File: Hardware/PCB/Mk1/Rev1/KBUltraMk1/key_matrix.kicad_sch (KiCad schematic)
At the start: 163 parts, among them SW1 SW_SPST, SW10 SW_SPST, SW11 SW_SPST, SW12 SW_SPST, SW13 SW_SPST, SW14 SW_SPST, SW15 SW_SPST, SW16 SW_SPST, SW17 SW_SPST, SW18 SW_SPST, SW19 SW_SPST, SW2 SW_SPST, SW20 SW_SPST, SW21 SW_SPST, SW22 SW_SPST, SW23 SW_SPST, SW24 SW_SPST, SW25 SW_SPST, SW26 SW_SPST, SW27 SW_SPST, SW28 SW_SPST, SW29 SW_SPST, SW3 SW_SPST, SW30 SW_SPST, SW31 SW_SPST, SW32 SW_SPST, SW33 SW_SPST, SW34 SW_SPST, SW35 SW_SPST, SW36 SW_SPST, SW37 SW_SPST, SW38 SW_SPST, SW39 SW_SPST, SW4 SW_SPST, SW40 SW_SPST, SW41 SW_SPST, SW42 SW_SPST, SW43 SW_SPST, SW44 SW_SPST, SW45 SW_SPST, SW46 SW_SPST, SW47 SW_SPST, SW48 SW_SPST, SW49 SW_SPST, SW5 SW_SPST, SW50 SW_SPST, SW51 SW_SPST, SW52 SW_SPST, SW53 SW_SPST, SW54 SW_SPST, SW55 SW_SPST, SW56 SW_SPST, SW57 SW_SPST, SW58 SW_SPST, SW59 SW_SPST, SW6 SW_SPST, SW60 SW_SPST, SW61 SW_SPST, SW62 SW_SPST, SW63 SW_SPST, SW64 SW_SPST, SW65 SW_SPST, SW66 SW_SPST, SW67 SW_SPST, SW68 SW_SPST, SW69 SW_SPST, SW7 SW_SPST, SW70 SW_SPST, SW71 SW_SPST, SW72 SW_SPST, SW73 SW_SPST, SW74 SW_SPST, SW75 SW_SPST, SW8 SW_SPST, SW9 SW_SPST

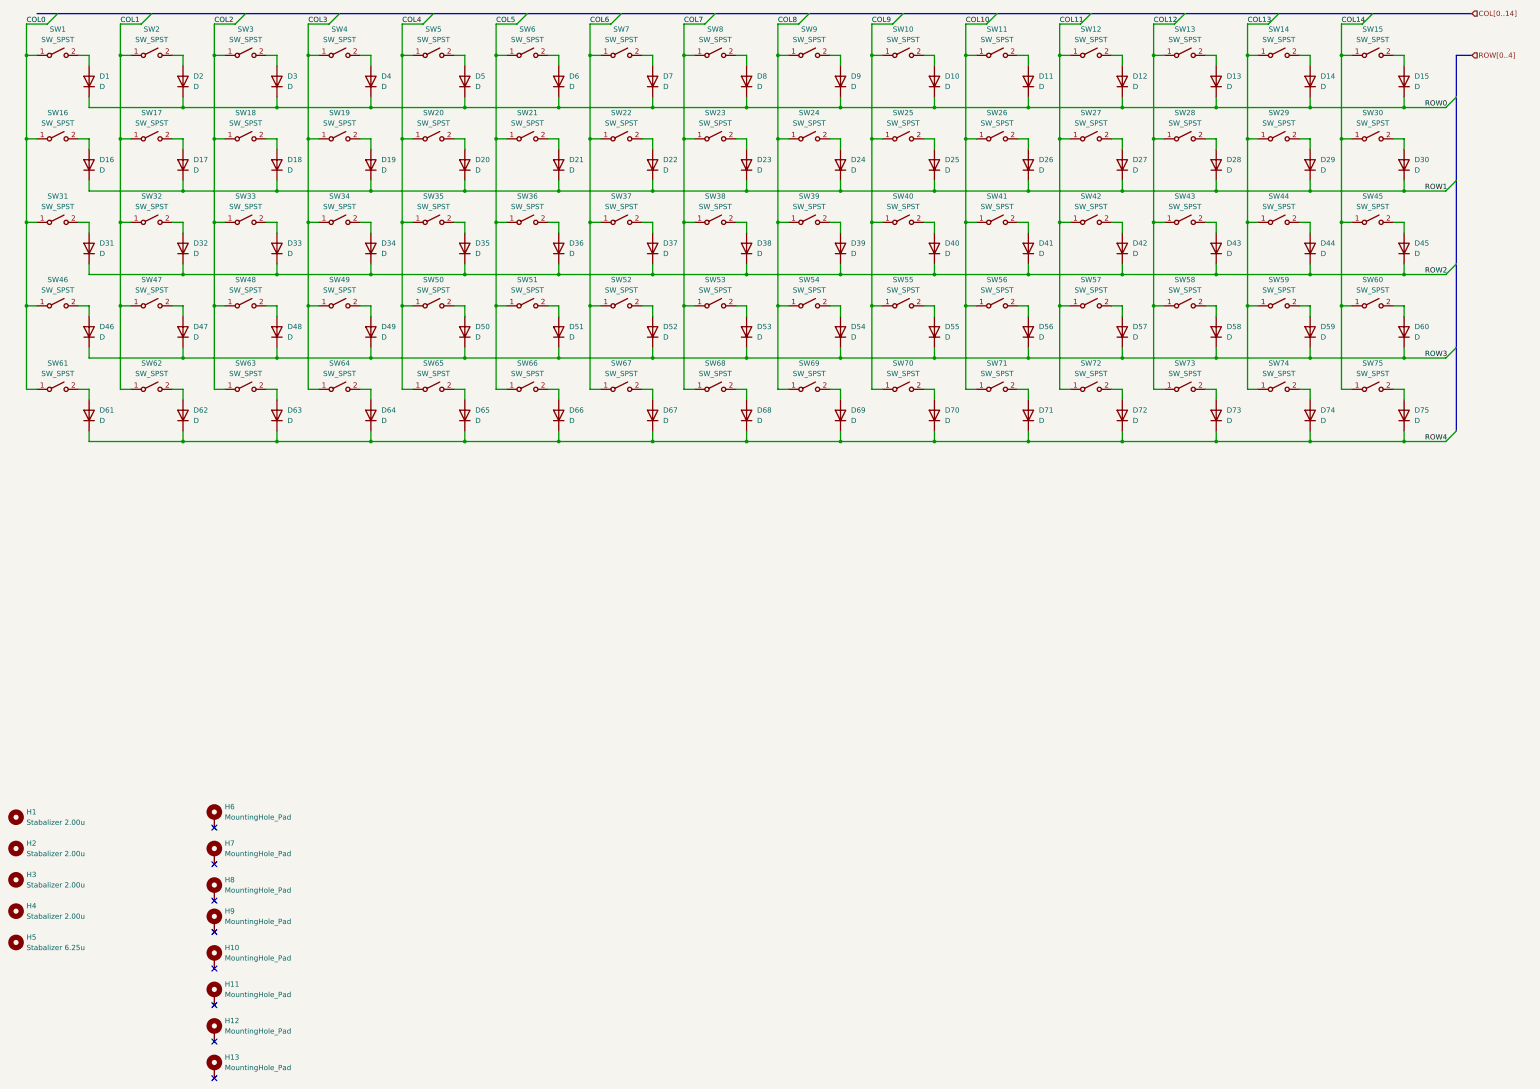
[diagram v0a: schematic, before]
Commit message: Added RP MCU
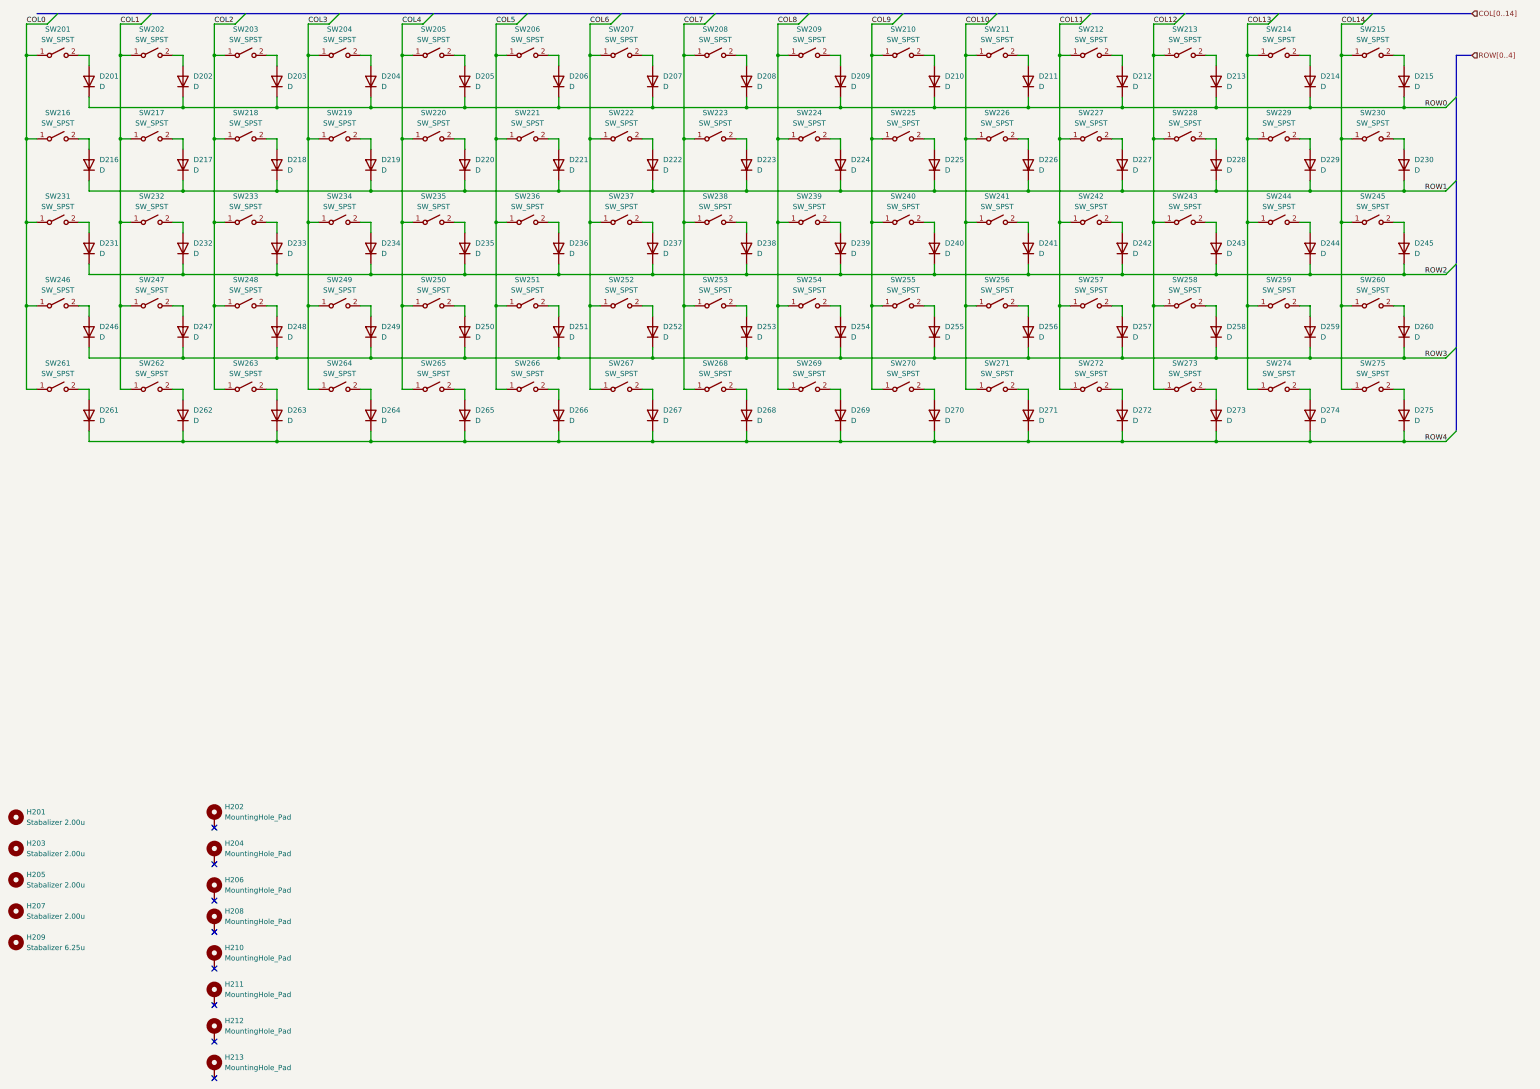
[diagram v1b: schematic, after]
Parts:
- renumbered D1 to D201, D2 to D202, D3 to D203, D4 to D204, D5 to D205, D6 to D206, D7 to D207, D8 to D208, D9 to D209, D10 to D210, D11 to D211, D12 to D212, D13 to D213, D14 to D214, D15 to D215, D16 to D216, D17 to D217, D18 to D218, D19 to D219, D20 to D220, D21 to D221, D22 to D222, D23 to D223, D24 to D224, D25 to D225, D26 to D226, D27 to D227, D28 to D228, D29 to D229, D30 to D230, D31 to D231, D32 to D232, D33 to D233, D34 to D234, D35 to D235, D36 to D236, D37 to D237, D38 to D238, D39 to D239, D40 to D240, D41 to D241, D42 to D242, D43 to D243, D44 to D244, D45 to D245, D46 to D246, D47 to D247, D48 to D248, D49 to D249, D50 to D250, D51 to D251, D52 to D252, D53 to D253, D54 to D254, D55 to D255, D56 to D256, D57 to D257, D58 to D258, D59 to D259, D60 to D260, D61 to D261, D62 to D262, D63 to D263, D64 to D264, D65 to D265, D66 to D266, D67 to D267, D68 to D268, D69 to D269, D70 to D270, D71 to D271, D72 to D272, D73 to D273, D74 to D274, D75 to D275, H1 to H201, H6 to H202, H2 to H203, H7 to H204, H3 to H205, H8 to H206, H4 to H207, H9 to H208, H5 to H209, H10 to H210, H11 to H211, H12 to H212, H13 to H213, SW1 to SW201, SW2 to SW202, SW3 to SW203, SW4 to SW204, SW5 to SW205, SW6 to SW206, SW7 to SW207, SW8 to SW208, SW9 to SW209, SW10 to SW210, SW11 to SW211, SW12 to SW212, SW13 to SW213, SW14 to SW214, SW15 to SW215, SW16 to SW216, SW17 to SW217, SW18 to SW218, SW19 to SW219, SW20 to SW220, SW21 to SW221, SW22 to SW222, SW23 to SW223, SW24 to SW224, SW25 to SW225, SW26 to SW226, SW27 to SW227, SW28 to SW228, SW29 to SW229, SW30 to SW230, SW31 to SW231, SW32 to SW232, SW33 to SW233, SW34 to SW234, SW35 to SW235, SW36 to SW236, SW37 to SW237, SW38 to SW238, SW39 to SW239, SW40 to SW240, SW41 to SW241, SW42 to SW242, SW43 to SW243, SW44 to SW244, SW45 to SW245, SW46 to SW246, SW47 to SW247, SW48 to SW248, SW49 to SW249, SW50 to SW250, SW51 to SW251, SW52 to SW252, SW53 to SW253, SW54 to SW254, SW55 to SW255, SW56 to SW256, SW57 to SW257, SW58 to SW258, SW59 to SW259, SW60 to SW260, SW61 to SW261, SW62 to SW262, SW63 to SW263, SW64 to SW264, SW65 to SW265, SW66 to SW266, SW67 to SW267, SW68 to SW268, SW69 to SW269, SW70 to SW270, SW71 to SW271, SW72 to SW272, SW73 to SW273, SW74 to SW274, SW75 to SW275
